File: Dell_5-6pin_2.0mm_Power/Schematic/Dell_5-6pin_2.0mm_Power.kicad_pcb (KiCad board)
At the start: 2 copper layers, 19.7 x 12.8 mm, 2 parts, among them J1 Dell Connector, J2 2.54mm Panel Header

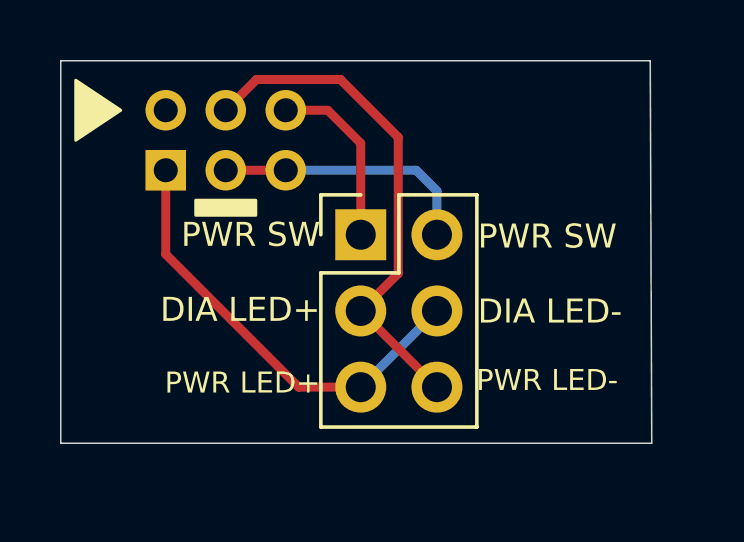
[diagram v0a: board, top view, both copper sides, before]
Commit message: redesigned to move the connectors further apart
In the previous version, the pins of the 2x3 2.54mm
connector bumped up against the shroud of the 2x3 2mm
connector on the motherboard. (Not so much that the
adapter didn't work, but still not ideal.)

The revised version reorients the 2x3 2.54mm header and
moves it a bit further from the 2mm connector.
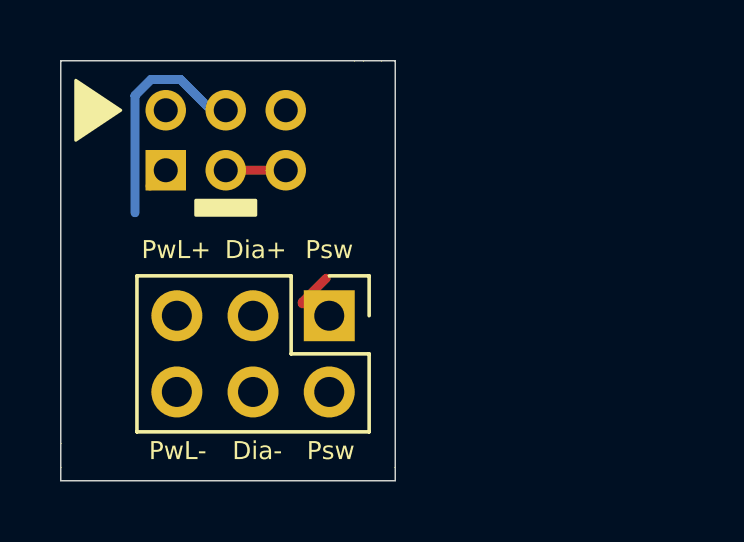
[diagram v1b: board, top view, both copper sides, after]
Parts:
- moved J2 2.90 mm to (164.9, 103.8), turned to 270 degrees
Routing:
- net DIAGNOSTIC_LED-: track 14.7 -> 0.75 mm
- net DIAGNOSTIC_LED+: track 16.9 -> 7.58 mm
- net POWER_SW_B: track 8.79 -> 2.00 mm
- net POWER_SW_A: track 6.01 -> 1.18 mm
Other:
- board size 19.7 x 12.8 mm -> 11.2 x 14 mm
- board text added: "Dia+"
- board text added: "Dia-"
- board text added: "Harbin Repairs 6p power btn adapter"
- board text added: "Psw"
- board text added: "PwL+"
- board text added: "PwL-"
- board text added: "daveho mod 4/22 github.com/daveho"
- board text removed: "DIA LED+"
- board text removed: "DIA LED-"
- board text removed: "PWR LED+"
- board text removed: "PWR LED-"
- board text removed: "PWR SW"
- board text removed: "Power Button Adapter For Dell 6p MB’s"
- board text removed: "daveho mod Feb 2022 github.com/daveho"
- board text removed: "github.com/ harbinrepairs"

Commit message: it helps if you actually route the signals, duh :-)
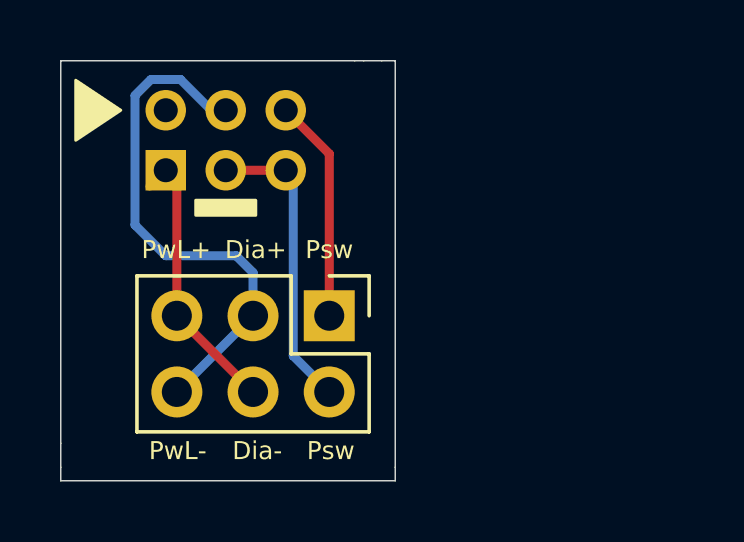
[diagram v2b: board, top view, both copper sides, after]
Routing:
- net DIAGNOSTIC_LED+: track 7.58 -> 17.6 mm
- net DIAGNOSTIC_LED-: track 0.75 -> 9.34 mm
- net POWER_SW_B: track 2.00 -> 9.99 mm
- net POWER_SW_A: track 1.18 -> 7.45 mm
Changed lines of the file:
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@@
     (thickness 1.6)
     (drawings 22)
-    (tracks 9)
+    (tracks 20)
     (zones 0)
     (modules 2)
@@
       (effects (font (size 1 1) (thickness 0.15)) (justify mirror))
     )
+    (fp_line (start -3.5 -5.5) (end -3.5 1.5) (layer B.CrtYd) (width 0.05))
+    (fp_line (start 1.5 -5.5) (end -3.5 -5.5) (layer B.CrtYd) (width 0.05))
+    (fp_line (start 1.5 1.5) (end 1.5 -5.5) (layer B.CrtYd) (width 0.05))
+    (fp_line (start -3.5 1.5) (end 1.5 1.5) (layer B.CrtYd) (width 0.05))
+    (fp_line (start 0 1.06) (end 1.06 1.06) (layer B.SilkS) (width 0.12))
+    (fp_line (start 1.06 1.06) (end 1.06 0) (layer B.SilkS) (width 0.12))
+    (fp_line (start -1 1.06) (end -1 -1) (layer B.SilkS) (width 0.12))
+    (fp_line (start -1 -1) (end 1.06 -1) (layer B.SilkS) (width 0.12))
+    (fp_line (start 1.06 -1) (end 1.06 -5.06) (layer B.SilkS) (width 0.12))
+    (fp_line (start -3.06 -5.06) (end 1.06 -5.06) (layer B.SilkS) (width 0.12))
+    (fp_line (start -3.06 1.06) (end -3.06 -5.06) (layer B.SilkS) (width 0.12))
+    (fp_line (start -3.06 1.06) (end -1 1.06) (layer B.SilkS) (width 0.12))
+    (fp_line (start -3 -5) (end -3 1) (layer B.Fab) (width 0.1))
+    (fp_line (start 1 -5) (end -3 -5) (layer B.Fab) (width 0.1))
+    (fp_line (start 1 0) (end 1 -5) (layer B.Fab) (width 0.1))
+    (fp_line (start 0 1) (end 1 0) (layer B.Fab) (width 0.1))
     (fp_line (start -3 1) (end 0 1) (layer B.Fab) (width 0.1))
-    (fp_line (start 0 1) (end 1 0) (layer B.Fab) (width 0.1))
-    (fp_line (start 1 0) (end 1 -5) (layer B.Fab) (width 0.1))
-    (fp_line (start 1 -5) (end -3 -5) (layer B.Fab) (width 0.1))
-    (fp_line (start -3 -5) (end -3 1) (layer B.Fab) (width 0.1))
-    (fp_line (start -3.06 1.06) (end -1 1.06) (layer B.SilkS) (width 0.12))
-    (fp_line (start -3.06 1.06) (end -3.06 -5.06) (layer B.SilkS) (width 0.12))
-    (fp_line (start -3.06 -5.06) (end 1.06 -5.06) (layer B.SilkS) (width 0.12))
-    (fp_line (start 1.06 -1) (end 1.06 -5.06) (layer B.SilkS) (width 0.12))
-    (fp_line (start -1 -1) (end 1.06 -1) (layer B.SilkS) (width 0.12))
-    (fp_line (start -1 1.06) (end -1 -1) (layer B.SilkS) (width 0.12))
-    (fp_line (start 1.06 1.06) (end 1.06 0) (layer B.SilkS) (width 0.12))
-    (fp_line (start 0 1.06) (end 1.06 1.06) (layer B.SilkS) (width 0.12))
-    (fp_line (start -3.5 1.5) (end 1.5 1.5) (layer B.CrtYd) (width 0.05))
-    (fp_line (start 1.5 1.5) (end 1.5 -5.5) (layer B.CrtYd) (width 0.05))
-    (fp_line (start 1.5 -5.5) (end -3.5 -5.5) (layer B.CrtYd) (width 0.05))
-    (fp_line (start -3.5 -5.5) (end -3.5 1.5) (layer B.CrtYd) (width 0.05))
     (fp_text user %R (at -1 -2 180) (layer B.Fab)
       (effects (font (size 1 1) (thickness 0.15)) (justify mirror))
@@
       (effects (font (size 1 1) (thickness 0.15)))
     )
+    (fp_line (start 4.35 -1.8) (end -1.8 -1.8) (layer F.CrtYd) (width 0.05))
+    (fp_line (start 4.35 6.85) (end 4.35 -1.8) (layer F.CrtYd) (width 0.05))
+    (fp_line (start -1.8 6.85) (end 4.35 6.85) (layer F.CrtYd) (width 0.05))
+    (fp_line (start -1.8 -1.8) (end -1.8 6.85) (layer F.CrtYd) (width 0.05))
+    (fp_line (start -1.33 -1.33) (end 0 -1.33) (layer F.SilkS) (width 0.12))
+    (fp_line (start -1.33 0) (end -1.33 -1.33) (layer F.SilkS) (width 0.12))
+    (fp_line (start 1.27 -1.33) (end 3.87 -1.33) (layer F.SilkS) (width 0.12))
+    (fp_line (start 1.27 1.27) (end 1.27 -1.33) (layer F.SilkS) (width 0.12))
+    (fp_line (start -1.33 1.27) (end 1.27 1.27) (layer F.SilkS) (width 0.12))
+    (fp_line (start 3.87 -1.33) (end 3.87 6.41) (layer F.SilkS) (width 0.12))
+    (fp_line (start -1.33 1.27) (end -1.33 6.41) (layer F.SilkS) (width 0.12))
+    (fp_line (start -1.33 6.41) (end 3.87 6.41) (layer F.SilkS) (width 0.12))
+    (fp_line (start -1.27 0) (end 0 -1.27) (layer F.Fab) (width 0.1))
+    (fp_line (start -1.27 6.35) (end -1.27 0) (layer F.Fab) (width 0.1))
+    (fp_line (start 3.81 6.35) (end -1.27 6.35) (layer F.Fab) (width 0.1))
+    (fp_line (start 3.81 -1.27) (end 3.81 6.35) (layer F.Fab) (width 0.1))
     (fp_line (start 0 -1.27) (end 3.81 -1.27) (layer F.Fab) (width 0.1))
-    (fp_line (start 3.81 -1.27) (end 3.81 6.35) (layer F.Fab) (width 0.1))
-    (fp_line (start 3.81 6.35) (end -1.27 6.35) (layer F.Fab) (width 0.1))
-    (fp_line (start -1.27 6.35) (end -1.27 0) (layer F.Fab) (width 0.1))
-    (fp_line (start -1.27 0) (end 0 -1.27) (layer F.Fab) (width 0.1))
-    (fp_line (start -1.33 6.41) (end 3.87 6.41) (layer F.SilkS) (width 0.12))
-    (fp_line (start -1.33 1.27) (end -1.33 6.41) (layer F.SilkS) (width 0.12))
-    (fp_line (start 3.87 -1.33) (end 3.87 6.41) (layer F.SilkS) (width 0.12))
-    (fp_line (start -1.33 1.27) (end 1.27 1.27) (layer F.SilkS) (width 0.12))
-    (fp_line (start 1.27 1.27) (end 1.27 -1.33) (layer F.SilkS) (width 0.12))
-    (fp_line (start 1.27 -1.33) (end 3.87 -1.33) (layer F.SilkS) (width 0.12))
-    (fp_line (start -1.33 0) (end -1.33 -1.33) (layer F.SilkS) (width 0.12))
-    (fp_line (start -1.33 -1.33) (end 0 -1.33) (layer F.SilkS) (width 0.12))
-    (fp_line (start -1.8 -1.8) (end -1.8 6.85) (layer F.CrtYd) (width 0.05))
-    (fp_line (start -1.8 6.85) (end 4.35 6.85) (layer F.CrtYd) (width 0.05))
-    (fp_line (start 4.35 6.85) (end 4.35 -1.8) (layer F.CrtYd) (width 0.05))
-    (fp_line (start 4.35 -1.8) (end -1.8 -1.8) (layer F.CrtYd) (width 0.05))
     (fp_text user %R (at 1.27 2.54) (layer F.Fab)
       (effects (font (size 1 1) (thickness 0.15)))
@@
   (gr_poly (pts (xy 158 97) (xy 156.5 98) (xy 156.5 96)) (layer B.SilkS) (width 0.1))
   (gr_poly (pts (xy 158 97) (xy 156.5 96) (xy 156.5 98)) (layer F.SilkS) (width 0.1))
-  (segment (start 164.05 103.45) (end 164.05 103.4) (width 0.3) (layer F.Cu) (net 1))
-  (segment (start 164.05 103.4) (end 164.85 102.6) (width 0.3) (layer F.Cu) (net 1))
-  (segment (start 158.474999 96.507999) (end 158.474999 100.414999) (width 0.3) (layer B.Cu) (net 2))
+  (segment (start 164.95 98.45) (end 163.5 97) (width 0.3) (layer F.Cu) (net 1))
+  (segment (start 164.95 103.85) (end 164.95 98.45) (width 0.3) (layer F.Cu) (net 1))
+  (segment (start 162.41 102.41) (end 162.41 103.85) (width 0.3) (layer B.Cu) (net 2))
+  (segment (start 159.5 101.85) (end 161.85 101.85) (width 0.3) (layer B.Cu) (net 2))
+  (segment (start 158.474999 100.824999) (end 159.5 101.85) (width 0.3) (layer B.Cu) (net 2))
+  (segment (start 161.85 101.85) (end 162.41 102.41) (width 0.3) (layer B.Cu) (net 2))
+  (segment (start 158.474999 96.507999) (end 158.474999 100.824999) (width 0.3) (layer B.Cu) (net 2))
   (segment (start 159.007999 95.974999) (end 158.474999 96.507999) (width 0.3) (layer B.Cu) (net 2))
   (segment (start 159.992001 95.974999) (end 159.007999 95.974999) (width 0.3) (layer B.Cu) (net 2))
   (segment (start 161.017002 97) (end 159.992001 95.974999) (width 0.3) (layer B.Cu) (net 2))
   (segment (start 161.5 97) (end 161.017002 97) (width 0.3) (layer B.Cu) (net 2))
+  (segment (start 162.41 103.85) (end 159.87 106.39) (width 0.3) (layer B.Cu) (net 2))
   (segment (start 159.5 99) (end 158.97 99.53) (width 0.3) (layer F.Cu) (net 3))
+  (segment (start 159.87 99.37) (end 159.5 99) (width 0.3) (layer F.Cu) (net 3))
+  (segment (start 159.87 103.85) (end 159.87 99.37) (width 0.3) (layer F.Cu) (net 3))
+  (segment (start 159.87 103.85) (end 162.41 106.39) (width 0.3) (layer F.Cu) (net 3))
   (segment (start 161.5 99) (end 163.5 99) (width 0.3) (layer F.Cu) (net 4))
+  (segment (start 163.75 99.25) (end 163.5 99) (width 0.3) (layer B.Cu) (net 4))
+  (segment (start 163.749999 105.189999) (end 163.75 99.25) (width 0.3) (layer B.Cu) (net 4))
+  (segment (start 164.95 106.39) (end 163.749999 105.189999) (width 0.3) (layer B.Cu) (net 4))
 )

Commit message: indicate top and bottom on silkscreen
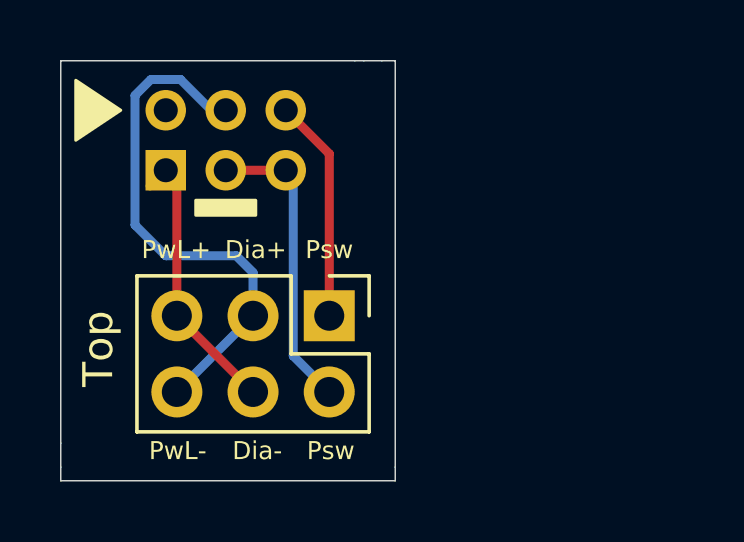
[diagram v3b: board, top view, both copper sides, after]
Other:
- board text added: "Bottom"
- board text added: "Top"
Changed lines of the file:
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@@
   (general
     (thickness 1.6)
-    (drawings 22)
+    (drawings 24)
     (tracks 20)
     (zones 0)
@@
       (effects (font (size 1 1) (thickness 0.15)) (justify mirror))
     )
+    (fp_line (start -3 1) (end 0 1) (layer B.Fab) (width 0.1))
+    (fp_line (start 0 1) (end 1 0) (layer B.Fab) (width 0.1))
+    (fp_line (start 1 0) (end 1 -5) (layer B.Fab) (width 0.1))
+    (fp_line (start 1 -5) (end -3 -5) (layer B.Fab) (width 0.1))
+    (fp_line (start -3 -5) (end -3 1) (layer B.Fab) (width 0.1))
+    (fp_line (start -3.06 1.06) (end -1 1.06) (layer B.SilkS) (width 0.12))
+    (fp_line (start -3.06 1.06) (end -3.06 -5.06) (layer B.SilkS) (width 0.12))
+    (fp_line (start -3.06 -5.06) (end 1.06 -5.06) (layer B.SilkS) (width 0.12))
+    (fp_line (start 1.06 -1) (end 1.06 -5.06) (layer B.SilkS) (width 0.12))
+    (fp_line (start -1 -1) (end 1.06 -1) (layer B.SilkS) (width 0.12))
+    (fp_line (start -1 1.06) (end -1 -1) (layer B.SilkS) (width 0.12))
+    (fp_line (start 1.06 1.06) (end 1.06 0) (layer B.SilkS) (width 0.12))
+    (fp_line (start 0 1.06) (end 1.06 1.06) (layer B.SilkS) (width 0.12))
+    (fp_line (start -3.5 1.5) (end 1.5 1.5) (layer B.CrtYd) (width 0.05))
+    (fp_line (start 1.5 1.5) (end 1.5 -5.5) (layer B.CrtYd) (width 0.05))
+    (fp_line (start 1.5 -5.5) (end -3.5 -5.5) (layer B.CrtYd) (width 0.05))
     (fp_line (start -3.5 -5.5) (end -3.5 1.5) (layer B.CrtYd) (width 0.05))
-    (fp_line (start 1.5 -5.5) (end -3.5 -5.5) (layer B.CrtYd) (width 0.05))
-    (fp_line (start 1.5 1.5) (end 1.5 -5.5) (layer B.CrtYd) (width 0.05))
-    (fp_line (start -3.5 1.5) (end 1.5 1.5) (layer B.CrtYd) (width 0.05))
-    (fp_line (start 0 1.06) (end 1.06 1.06) (layer B.SilkS) (width 0.12))
-    (fp_line (start 1.06 1.06) (end 1.06 0) (layer B.SilkS) (width 0.12))
-    (fp_line (start -1 1.06) (end -1 -1) (layer B.SilkS) (width 0.12))
-    (fp_line (start -1 -1) (end 1.06 -1) (layer B.SilkS) (width 0.12))
-    (fp_line (start 1.06 -1) (end 1.06 -5.06) (layer B.SilkS) (width 0.12))
-    (fp_line (start -3.06 -5.06) (end 1.06 -5.06) (layer B.SilkS) (width 0.12))
-    (fp_line (start -3.06 1.06) (end -3.06 -5.06) (layer B.SilkS) (width 0.12))
-    (fp_line (start -3.06 1.06) (end -1 1.06) (layer B.SilkS) (width 0.12))
-    (fp_line (start -3 -5) (end -3 1) (layer B.Fab) (width 0.1))
-    (fp_line (start 1 -5) (end -3 -5) (layer B.Fab) (width 0.1))
-    (fp_line (start 1 0) (end 1 -5) (layer B.Fab) (width 0.1))
-    (fp_line (start 0 1) (end 1 0) (layer B.Fab) (width 0.1))
-    (fp_line (start -3 1) (end 0 1) (layer B.Fab) (width 0.1))
     (fp_text user %R (at -1 -2 180) (layer B.Fab)
       (effects (font (size 1 1) (thickness 0.15)) (justify mirror))
@@
       (effects (font (size 1 1) (thickness 0.15)))
     )
+    (fp_line (start 0 -1.27) (end 3.81 -1.27) (layer F.Fab) (width 0.1))
+    (fp_line (start 3.81 -1.27) (end 3.81 6.35) (layer F.Fab) (width 0.1))
+    (fp_line (start 3.81 6.35) (end -1.27 6.35) (layer F.Fab) (width 0.1))
+    (fp_line (start -1.27 6.35) (end -1.27 0) (layer F.Fab) (width 0.1))
+    (fp_line (start -1.27 0) (end 0 -1.27) (layer F.Fab) (width 0.1))
+    (fp_line (start -1.33 6.41) (end 3.87 6.41) (layer F.SilkS) (width 0.12))
+    (fp_line (start -1.33 1.27) (end -1.33 6.41) (layer F.SilkS) (width 0.12))
+    (fp_line (start 3.87 -1.33) (end 3.87 6.41) (layer F.SilkS) (width 0.12))
+    (fp_line (start -1.33 1.27) (end 1.27 1.27) (layer F.SilkS) (width 0.12))
+    (fp_line (start 1.27 1.27) (end 1.27 -1.33) (layer F.SilkS) (width 0.12))
+    (fp_line (start 1.27 -1.33) (end 3.87 -1.33) (layer F.SilkS) (width 0.12))
+    (fp_line (start -1.33 0) (end -1.33 -1.33) (layer F.SilkS) (width 0.12))
+    (fp_line (start -1.33 -1.33) (end 0 -1.33) (layer F.SilkS) (width 0.12))
+    (fp_line (start -1.8 -1.8) (end -1.8 6.85) (layer F.CrtYd) (width 0.05))
+    (fp_line (start -1.8 6.85) (end 4.35 6.85) (layer F.CrtYd) (width 0.05))
+    (fp_line (start 4.35 6.85) (end 4.35 -1.8) (layer F.CrtYd) (width 0.05))
     (fp_line (start 4.35 -1.8) (end -1.8 -1.8) (layer F.CrtYd) (width 0.05))
-    (fp_line (start 4.35 6.85) (end 4.35 -1.8) (layer F.CrtYd) (width 0.05))
-    (fp_line (start -1.8 6.85) (end 4.35 6.85) (layer F.CrtYd) (width 0.05))
-    (fp_line (start -1.8 -1.8) (end -1.8 6.85) (layer F.CrtYd) (width 0.05))
-    (fp_line (start -1.33 -1.33) (end 0 -1.33) (layer F.SilkS) (width 0.12))
-    (fp_line (start -1.33 0) (end -1.33 -1.33) (layer F.SilkS) (width 0.12))
-    (fp_line (start 1.27 -1.33) (end 3.87 -1.33) (layer F.SilkS) (width 0.12))
-    (fp_line (start 1.27 1.27) (end 1.27 -1.33) (layer F.SilkS) (width 0.12))
-    (fp_line (start -1.33 1.27) (end 1.27 1.27) (layer F.SilkS) (width 0.12))
-    (fp_line (start 3.87 -1.33) (end 3.87 6.41) (layer F.SilkS) (width 0.12))
-    (fp_line (start -1.33 1.27) (end -1.33 6.41) (layer F.SilkS) (width 0.12))
-    (fp_line (start -1.33 6.41) (end 3.87 6.41) (layer F.SilkS) (width 0.12))
-    (fp_line (start -1.27 0) (end 0 -1.27) (layer F.Fab) (width 0.1))
-    (fp_line (start -1.27 6.35) (end -1.27 0) (layer F.Fab) (width 0.1))
-    (fp_line (start 3.81 6.35) (end -1.27 6.35) (layer F.Fab) (width 0.1))
-    (fp_line (start 3.81 -1.27) (end 3.81 6.35) (layer F.Fab) (width 0.1))
-    (fp_line (start 0 -1.27) (end 3.81 -1.27) (layer F.Fab) (width 0.1))
     (fp_text user %R (at 1.27 2.54) (layer F.Fab)
       (effects (font (size 1 1) (thickness 0.15)))
@@
     )
   )
+  (gr_text Bottom (at 161.85 108.25) (layer B.SilkS)
+    (effects (font (size 1 1) (thickness 0.15)) (justify mirror))
+  )
+  (gr_text Top (at 157.25 104.95 90) (layer F.SilkS)
+    (effects (font (size 1 1) (thickness 0.15)))
+  )
   (gr_line (start 167.15 109.35) (end 167.15 108.9) (layer Edge.Cuts) (width 0.05))
